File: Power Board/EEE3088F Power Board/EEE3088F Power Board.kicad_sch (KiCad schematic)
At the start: 91 parts, among them J1 Conn_02x16_Odd_Even, J2 USB_C_Receptacle, J3 Conn_01x02_Socket, Q1 2N7002, SW1 SW_SPDT_312, U1 INA219AIDCNR, U10 AP22966DC8-7, U2 LM2596SX-5.0/NOPB, U3 TP4056-42-ESOP8, U4 DRV8837, U5 DRV8837, U6 DRV8837, U8 DRV8837, U9 CH224K

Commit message: more labels and footprints
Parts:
- added JP_M_3V3: 3V3_VM, Jumper:SolderJumper-2_P1.3mm_Open_RoundedPad1.0x1.5mm, symbol Jumper:SolderJumper_2_Open
- D2: value LED -> Red LED; footprint (none) -> LED_SMD:LED_0603_1608Metric_Pad1.05x0.95mm_HandSolder; JLCPCB Part # (none) -> C2286
- D3: value LED -> Green LED; footprint (none) -> LED_SMD:LED_0805_2012Metric_Pad1.15x1.40mm_HandSolder; JLCPCB Part # (none) -> C2297
- L_Bin: renamed from L1; JLCPCB Part # (none) -> C2924827
- renumbered C4 to C_B1, C5 to C_B2, C2 to C_Bin, C3 to C_Bout, C13 to C_C_dd, D1 to D_Bskt, R13 to R_B_LED1, R12 to R_B_LED2, R16 to R_B_b, R14 to R_B_fast, R17 to R_B_pd, R15 to R_B_slow, R23 to R_C_bus, R24 to R_C_cfg, R22 to R_C_dd
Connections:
- net +3V3: now also JP_M_3V3.2 (B); no longer U4.7 (~{SLEEP}), U4.8 (VCC), U5.7 (~{SLEEP}), U5.8 (VCC), U6.7 (~{SLEEP}), U6.8 (VCC), U8.7 (~{SLEEP}), U8.8 (VCC)
- new net 3V3_M: JP_M_3V3.1 (A), U4.7 (~{SLEEP}), U4.8 (VCC), U5.7 (~{SLEEP}), U5.8 (VCC), U6.7 (~{SLEEP}), U6.8 (VCC), U8.7 (~{SLEEP}), U8.8 (VCC)
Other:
- note added: "Do capacitor and inductor values need to be exact? Save budget If so, is it worth changing my whole design to find a different buck convertor that doesn't use extended caps"
- note added: "Done: - Resistors and Capacitors footprints (except LM256) - IC footprints - Schottky diode and 2N7002 footprints - LED footprints To Do: - LM256 caps and inductor? - ask about 0.4R resistor - Neaten net labels - relabel passive components"
- note added: "found a 22uH extended preferred but stock count 307??"
- note removed: "Do capacitor and inductor values need to be exact? Save budget"
- note removed: "Done: - Resistors and Capacitors footprints (except LM256) - IC footprints - Schottky diode and 2N7002 footprints To Do: - LED footprints - LM256 caps and inductor? - ask about 0.4R resistor - Neaten net labels - relabel passive components"
- moved on the sheet: D2, R_B_LED1, U4, U5, U6, U8

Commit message: notes and checked. SW FP to o
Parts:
- removed SW1: SW_SPDT_312, symbol Switch:SW_SPDT_312
- removed TP20: TestPoint, TestPoint:TestPoint_Pad_D2.0mm, symbol Connector:TestPoint
- added JPI4: VIN1, Jumper:SolderJumper-2_P1.3mm_Open_RoundedPad1.0x1.5mm, symbol Jumper:SolderJumper_2_Open
- added JPI5: VIN2, Jumper:SolderJumper-2_P1.3mm_Open_RoundedPad1.0x1.5mm, symbol Jumper:SolderJumper_2_Open
- added JPI6: VBIAS, Jumper:SolderJumper-2_P1.3mm_Open_RoundedPad1.0x1.5mm, symbol Jumper:SolderJumper_2_Open
- added JP_P3: LDO_PWR, Jumper:SolderJumper-2_P1.3mm_Open_RoundedPad1.0x1.5mm, symbol Jumper:SolderJumper_2_Open
- added SW2: ~, ProLib_pcs_2025-03-25:SW-TH_SS-12D11G5, symbol ProLib_pcs_2025-03-25:SS-12D11G5
- C15: footprint Capacitor_SMD:C_0402_1005Metric_Pad0.74x0.62mm_HandSolder -> Capacitor_SMD:C_0603_1608Metric_Pad1.08x0.95mm_HandSolder
- C16: footprint (none) -> Capacitor_SMD:C_0201_0603Metric_Pad0.64x0.40mm_HandSolder
- C25: footprint Capacitor_SMD:C_0402_1005Metric_Pad0.74x0.62mm_HandSolder -> Capacitor_SMD:C_0201_0603Metric_Pad0.64x0.40mm_HandSolder
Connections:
- net +3V3: now also JPI6.2 (B); no longer TP21.1, U10.4 (VBIAS)
- net +5V: now also JPI4.2 (B), JPI5.2 (B), JP_P3.2 (B); no longer C15.1, C25.1, C_P(in)1.2, U10.1_2 (VIN1), U10.6_7 (VIN2), U_P2.3 (VI)
- net Battery: now also SW2.1; no longer JP_P1.2 (B)
- net GND: now also SW2.3
- net Switch-: now also JP_P1.2 (B), SW2.2
- new net: JPI6.1 (A), TP21.1, U10.4 (VBIAS)
- new net: C25.1, JPI4.1 (A), U10.1_2 (VIN1)
- new net: C15.1, JPI5.1 (A), U10.6_7 (VIN2)
- new net: C_P(in)1.2, JP_P3.1 (A), U_P2.3 (VI)
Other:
- note added: "- Double check the Ciss Cap values - Correct symbol - EXT is for base thermal - Add LED indicator."
- note added: "Acceptance Testing - Check shunt res - Vcc solder - Check not overheating - Solder i2c - connect stm Fix: -solder across shunt / replc"
- note added: "Acceptance Testing - solder Boost_mode - solder Boostpwr - Check output tp - Check FB V - Load output Fix: - Change L - Change R"
- note added: "Acceptance Testing - solder PWR - Check output V - LED on - Load output Fix: - Manual 3v3 line - V div"
- note added: "Acceptance testing: - Check correct orientation - Plug in and check V w/ TP Fixing: - Reverse the wires on the batt conn"
- note added: "Acceptance testing: - Solder Vbias - Scheck - Solder VIN1 - CHECK - TOGGLE INPUT - CHECK - repeat EN2 Fixing: - Take the L"
- note added: "Acceptance testing: - With out battery - Check for SC test with multimeter Fixing: - Pull of and solder man"
- note removed: "- Double check the Cap values - What is EXP? Base plate contact maybe - Check this is 100% the right symbol. The other pins are correct, just concerend abt 15 - I think this is the packafe with exposed PAD for thermal - base - Add LED indicator?"
- note removed: "Acceptance Testing - LED will show good power - Test point to measure voltage - Add connection for external load to drive (think Res bank)"

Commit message: added footprints and fixed buck
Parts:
- removed C_Bin: 680uF, symbol Device:C
- removed C_Bout: 220uF, symbol Device:C
- removed D_Bskt: SS54, Diode_SMD:D_SMA, symbol Diode:SS34
- removed JP1: SolderJumper_2_Open, symbol Jumper:SolderJumper_2_Open
- removed L_Bin: 22uH, symbol Device:L
- removed R11: 1, Resistor_SMD:R_0402_1005Metric_Pad0.72x0.64mm_HandSolder, symbol Device:R_US
- removed R18, R21: 0.1R, Resistor_SMD:R_1206_3216Metric_Pad1.30x1.75mm_HandSolder, symbol Device:R_US
- removed TP16, TP5: TestPoint, TestPoint:TestPoint_Pad_D2.0mm, symbol Connector:TestPoint
- removed U2: LM2596SX-5.0/NOPB, LM2596SX-5.0_NOPB:VREG_LM2596SX-5.0_NOPB, symbol Regulator_Switching:LM2596S-5
- added C1: 10uF, Capacitor_SMD:C_1206_3216Metric_Pad1.33x1.80mm_HandSolder, symbol Device:C_Small
- added C2: 10nF, Capacitor_SMD:C_0603_1608Metric_Pad1.08x0.95mm_HandSolder, symbol Device:C_Small
- added C3: 220uF, Capacitor_SMD:CP_Elec_6.3x7.7, symbol Device:C_Small
- added D1: B340, B340A:SMA-DIODE, symbol Diode:B340
- added L1: 18uH, Inductor_SMD:L_Abracon_ASPI-4030S, symbol Device:L_Small
- added R1: 10k, Resistor_SMD:R_0603_1608Metric_Pad0.98x0.95mm_HandSolder, symbol Device:R_Small_US
- added R2: 3k3, Resistor_SMD:R_0603_1608Metric_Pad0.98x0.95mm_HandSolder, symbol Device:R_Small_US
- added U2: TPS5430DDA, Package_SO:SOIC-8-1EP_3.9x4.9mm_P1.27mm_EP2.29x3mm, symbol Regulator_Switching:TPS5430DDA
- D5: footprint (none) -> LED_SMD:LED_0805_2012Metric_Pad1.15x1.40mm_HandSolder
- J1: footprint (none) -> Connector_PinHeader_2.54mm:PinHeader_2x16_P2.54mm_Vertical
- J2: footprint (none) -> Connector_USB:USB_C_Receptacle_G-Switch_GT-USB-7010ASV
- L3: footprint (none) -> Inductor_SMD:L_Changjiang_FXL0630
- R19, R20: value 0.1R -> 1R; footprint Resistor_SMD:R_1206_3216Metric_Pad1.30x1.75mm_HandSolder -> Resistor_SMD:R_0603_1608Metric_Pad0.98x0.95mm_HandSolder
- R_Pfb1: value 732k -> 510k
- R_Pfb2: value 100k -> 68k
- renumbered Batt+ to Batt+1, Batt- to Batt-1, C_C_dd to C_C_dd1, C_I(in) to C_I(in)1, C_P(in) to C_P(in)3, R_B_b to R_B_b1, R_B_fast to R_B_fast1, R_B_pd to R_B_pd1, R_B_slow to R_B_slow1, R_C_bus to R_C_bus1, R_C_cfg to R_C_cfg1, R_C_dd to R_C_dd1, R_Ishunt to R_Ishunt1
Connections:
- net 5V Out is gone; now on net +5V: J1.20 (Pin_20)
- net 5V_Buck_Out: now also R19.1, R20.1, C3.1, L1.2, R1.1; no longer TP17.1
- net GND: now also C1.2, C3.2, D1.2 (A), R2.2, U2.6 (GND), U2.9 (GNDPAD)
- net HV: now also C1.1, U2.7 (VIN)
- net at C_B1.1, D2.2 (A), D3.2 (A)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: now also R19.2, R20.2
- net RESV: no longer names the net of J1.15 (Pin_15)
- net USART2_RX: no longer names the net of J1.9 (Pin_9)
- net USART2_TX: no longer names the net of J1.12 (Pin_12)
- new net: R1.2, R2.1, TP17.1, U2.4 (VSENSE)
- new net: C2.1, U2.1 (BOOT)
- new net: C2.2, D1.1 (K), L1.1, U2.8 (PH)
- no-connect marks 14 -> 18
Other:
- note added: "**fix footprint"
- note added: "Can't find basic 0.4R resistor, can only find basic 1R make 0.5R using parallel"
- note added: "REMEBER TO ASSIGN CORRECT FOOTPRINT"
- note added: "RESV"
- note added: "USART2_RX"
- note added: "USART2_TX"
- note removed: "Can't find basic 0.4R resistor, can only find basic 0.1R"
- note removed: "To copy (Justin values) Foot prints set"
- moved on the sheet: C_B1, C_B2, D2, D3, Q1, R19, R_B_LED1, R_B_LED2, R_B_b1, R_B_fast1, R_B_pd1, R_B_slow1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

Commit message: rip
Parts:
- C16, C25: footprint Capacitor_SMD:C_0201_0603Metric_Pad0.64x0.40mm_HandSolder -> Capacitor_SMD:C_0603_1608Metric_Pad1.08x0.95mm_HandSolder
- SW2: footprint ProLib_pcs_2025-03-25:SW-TH_SS-12D11G5 -> Button_Switch_SMD:SW_SPDT_CK_JS102011SAQN
- U10: footprint AP22966DC8-7:IC_AP22966DC8-7 -> Imported_Files:IC_AP22966DC8-7
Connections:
- net Motor1_A_OUT is gone; now on net MOTOR1_A_OUT: U8.2 (OUT1)
- net Motor1_B_OUT is gone; now on net MOTOR1_B_OUT: U8.3 (OUT2)
- net Motor3_A_OUT is gone; now on net MOTOR3_A_OUT: U6.2 (OUT1)
- net Motor3_B_OUT is gone; now on net MOTOR3_B_OUT: U6.3 (OUT2)
- net MOTOR3_B OUT renamed MOTOR3_A_OUT
- net Motor2_A_OUT renamed MOTOR2_A_OUT
- net Motor2_B_OUT renamed MOTOR2_B_OUT
- net Motor4_A_OUT renamed MOTOR4_A_OUT
- net Motor4_B_OUT renamed MOTOR4_B_OUT
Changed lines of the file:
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@@
 	(text "Do capacitor and inductor values \nneed to be exact? Save budget\nIf so, is it worth changing my whole design \nto find a different buck convertor that \ndoesn't use extended caps"
 		(exclude_from_sim no)
-		(at 214.884 189.992 0)
+		(at 252.476 180.848 0)
 		(effects
 			(font
@@
 	)
 	(junction
-		(at 231.14 187.96)
-		(diameter 0)
-		(color 0 0 0 0)
-	)
-	(junction
 		(at 229.87 57.15)
 		(diameter 0)
@@
 	)
 	(junction
-		(at 269.24 57.15)
-		(diameter 0)
-		(color 0 0 0 0)
-	)
-	(junction
 		(at 386.08 189.23)
 		(diameter 0)
@@
 	(wire
 		(pts
-			(xy 231.14 187.96) (xy 231.14 181.61)
-		)
-		(stroke
-			(width 0)
-			(type default)
-		)
-	)
-	(wire
-		(pts
 			(xy 297.18 149.86) (xy 297.18 151.13)
 		)
@@
 	(wire
 		(pts
-			(xy 269.24 52.07) (xy 269.24 57.15)
-		)
-		(stroke
-			(width 0)
-			(type default)
-		)
-	)
-	(wire
-		(pts
 			(xy 386.08 189.23) (xy 386.08 199.39)
 		)
@@
 	(wire
 		(pts
-			(xy 259.08 57.15) (xy 269.24 57.15)
-		)
-		(stroke
-			(width 0)
-			(type default)
-		)
-	)
-	(wire
-		(pts
 			(xy 464.82 40.64) (xy 464.82 35.56)
 		)
@@
 	(wire
 		(pts
-			(xy 231.14 173.99) (xy 231.14 172.72)
-		)
-		(stroke
-			(width 0)
-			(type default)
-		)
-	)
-	(wire
-		(pts
 			(xy 154.94 179.07) (xy 171.45 179.07)
 		)
@@
 	(wire
 		(pts
-			(xy 231.14 189.23) (xy 231.14 187.96)
-		)
-		(stroke
-			(width 0)
-			(type default)
-		)
-	)
-	(wire
-		(pts
 			(xy 194.31 246.38) (xy 200.66 246.38)
 		)
@@
 	(wire
 		(pts
-			(xy 269.24 57.15) (xy 279.4 57.15)
+			(xy 259.08 57.15) (xy 279.4 57.15)
 		)
 		(stroke
@@
 	(wire
 		(pts
-			(xy 231.14 187.96) (xy 241.3 187.96)
-		)
-		(stroke
-			(width 0)
-			(type default)
-		)
-	)
-	(wire
-		(pts
 			(xy 273.05 143.51) (xy 279.4 143.51)
 		)
@@
 		)
 	)
-	(label "Motor2_B_OUT"
+	(label "MOTOR2_B_OUT"
 		(at 154.94 148.59 0)
 		(effects
@@
 		)
 	)
-	(label "3V3 Out"
-		(at 269.24 52.07 0)
-		(effects
-			(font
-				(size 1.27 1.27)
-			)
-			(justify left bottom)
-		)
-	)
-	(label "Motor1_A_OUT"
+	(label "MOTOR1_A_OUT"
 		(at 482.6 92.71 0)
 		(effects
@@
 		)
 	)
-	(label "MOTOR3_B OUT"
+	(label "MOTOR3_A_OUT"
 		(at 156.21 181.61 0)
 		(effects
@@
 		)
 	)
-	(label "Motor4_B_OUT"
+	(label "MOTOR4_B_OUT"
 		(at 553.72 59.69 0)
 		(effects
@@
 		)
 	)
-	(label "Motor2_B_OUT"
+	(label "MOTOR2_B_OUT"
 		(at 481.33 60.96 0)
 		(effects
@@
 		)
 	)
-	(label "Motor3_B_OUT"
+	(label "MOTOR3_B_OUT"
 		(at 554.99 105.41 0)
 		(effects
@@
 		)
 	)
-	(label "Motor1_B_OUT"
+	(label "MOTOR1_B_OUT"
 		(at 482.6 107.95 0)
 		(effects
@@
 		)
 	)
-	(label "Motor2_A_OUT"
+	(label "MOTOR2_A_OUT"
 		(at 490.22 45.72 0)
 		(effects
@@
 		)
 	)
-	(label "Motor2_A_OUT"
+	(label "MOTOR2_A_OUT"
 		(at 186.69 148.59 0)
 		(effects
@@
 		)
 	)
-	(label "Motor3_A_OUT"
+	(label "MOTOR3_A_OUT"
 		(at 554.99 90.17 0)
 		(effects
@@
 		)
 	)
-	(label "Motor4_A_OUT"
+	(label "MOTOR4_A_OUT"
 		(at 562.61 44.45 0)
 		(effects
@@
 		)
 	)
-	(label "Motor4_A_OUT"
+	(label "MOTOR4_A_OUT"
 		(at 154.94 151.13 0)
 		(effects
@@
 			)
 		)
-		(property "Footprint" "ProLib_pcs_2025-03-25:SW-TH_SS-12D11G5"
+		(property "Footprint" "Button_Switch_SMD:SW_SPDT_CK_JS102011SAQN"
 			(at 69.85 327.66 0)
 			(effects
@@
 			)
 		)
-		(property "Footprint" "AP22966DC8-7:IC_AP22966DC8-7"
+		(property "Footprint" "Imported_Files:IC_AP22966DC8-7"
 			(at 71.12 238.76 0)
 			(effects
@@
 	)
 	(symbol
-		(lib_id "power:GND")
-		(at 231.14 189.23 0)
-		(unit 1)
-		(exclude_from_sim no)
-		(in_bom yes)
-		(on_board yes)
-		(dnp no)
-		(fields_autoplaced yes)
-		(property "Reference" "#PWR04"
-			(at 231.14 195.58 0)
-			(effects
-				(font
-					(size 1.27 1.27)
-				)
-				(hide yes)
-			)
-		)
-		(property "Value" "GND"
-			(at 231.14 194.31 0)
-			(effects
-				(font
-					(size 1.27 1.27)
-				)
-			)
-		)
-		(property "Footprint" ""
-			(at 231.14 189.23 0)
-			(effects
-				(font
-					(size 1.27 1.27)
-				)
-				(hide yes)
-			)
-		)
-		(property "Datasheet" ""
-			(at 231.14 189.23 0)
-			(effects
-				(font
-					(size 1.27 1.27)
-				)
-				(hide yes)
-			)
-		)
-		(property "Description" "Power symbol creates a global label with name \"GND\" , ground"
-			(at 231.14 189.23 0)
-			(effects
-				(font
-					(size 1.27 1.27)
-				)
-				(hide yes)
-			)
-		)
-		(pin "1"
-		)
-		(instances
-			(project ""
-				(path "/713ead88-0bd2-43ee-981f-e11872ed406d"
-					(reference "#PWR04")
-					(unit 1)
-				)
-			)
-		)
-	)
-	(symbol
 		(lib_id "Device:L")
 		(at 95.25 50.8 90)
@@
 			)
 		)
-		(property "Footprint" "Capacitor_SMD:C_0201_0603Metric_Pad0.64x0.40mm_HandSolder"
+		(property "Footprint" "Capacitor_SMD:C_0603_1608Metric_Pad1.08x0.95mm_HandSolder"
 			(at 96.52 233.68 0)
 			(effects
@@
 			)
 		)
-		(property "Footprint" "Capacitor_SMD:C_0201_0603Metric_Pad0.64x0.40mm_HandSolder"
+		(property "Footprint" "Capacitor_SMD:C_0603_1608Metric_Pad1.08x0.95mm_HandSolder"
 			(at 21.59 233.68 0)
 			(effects

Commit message: Fixed communal fp and symbols
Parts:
- removed SW2: ~, Button_Switch_SMD:SW_SPDT_CK_JS102011SAQN, symbol ProLib_pcs_2025-03-25:SS-12D11G5
- removed U10: AP22966DC8-7, Imported_Files:IC_AP22966DC8-7, symbol AP22966DC8-7:AP22966DC8-7
- added SW1: ~, custom_footprints:SW-TH_SS-12D11G5, symbol Custom_symbols:SS-12D11G5
- added U7: AP22966DC8-7, custom_footprints:IC_AP22966DC8-7, symbol Custom_symbols:AP22966DC8-7
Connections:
- net Battery: now also SW1.1
- net CTRL_EXT_LOAD1: now also U7.3 (EN1)
- net CTRL_EXT_LOAD2: now also U7.5 (EN2)
- net EXT_LOAD1_OUT: now also U7.13_14 (VOUT1)
- net EXT_LOAD2_OUT: now also U7.8_9 (VOUT2)
- net GND: now also SW1.3, U7.11 (GND), U7.15 (EXP)
- net Switch-: now also SW1.2
- net at JPI6.1 (A), TP21.1: now also U7.4 (VBIAS)
- net at C17.2: now also U7.10 (SS2)
- net at C16.2: now also U7.12 (SS1)
- net at C25.1, JPI4.1 (A): now also U7.1_2 (VIN1)
- net at C15.1, JPI5.1 (A): now also U7.6_7 (VIN2)

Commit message: ELC checks
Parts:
- D1: footprint B340A:SMA-DIODE -> custom_footprints:SMA-DIODE
- U3: footprint TP4056-42-ESOP8:SOIC127P600X175-9N -> custom_footprints:SOIC127P600X175-9N
- U4, U5, U6, U8: footprint DRV8837DSGR:SON50P200X200X80-9N -> custom_footprints:SON50P200X200X80-9N
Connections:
- net +3V3 is gone; now on net +3.3V: C_P(in)2.2, J1.18 (Pin_18), JPI6.2 (B), JP_M_3V3.2 (B), R_P2.1, TP_P6.1, U_P2.2 (VO)
- net MOTOR4_B_OUT_ is gone; now on net MOTOR4_B_OUT: J1.5 (Pin_5)
- net HV: no longer J1.22 (Pin_22), J2.A4 (VBUS), J2.A9 (VBUS), J2.B4 (VBUS), J2.B9 (VBUS), R_C_bus1.1, R_C_dd1.1, TP6.1
- new net +9V: J1.22 (Pin_22), J2.A4 (VBUS), J2.A9 (VBUS), J2.B4 (VBUS), J2.B9 (VBUS), R_C_bus1.1, R_C_dd1.1, TP6.1

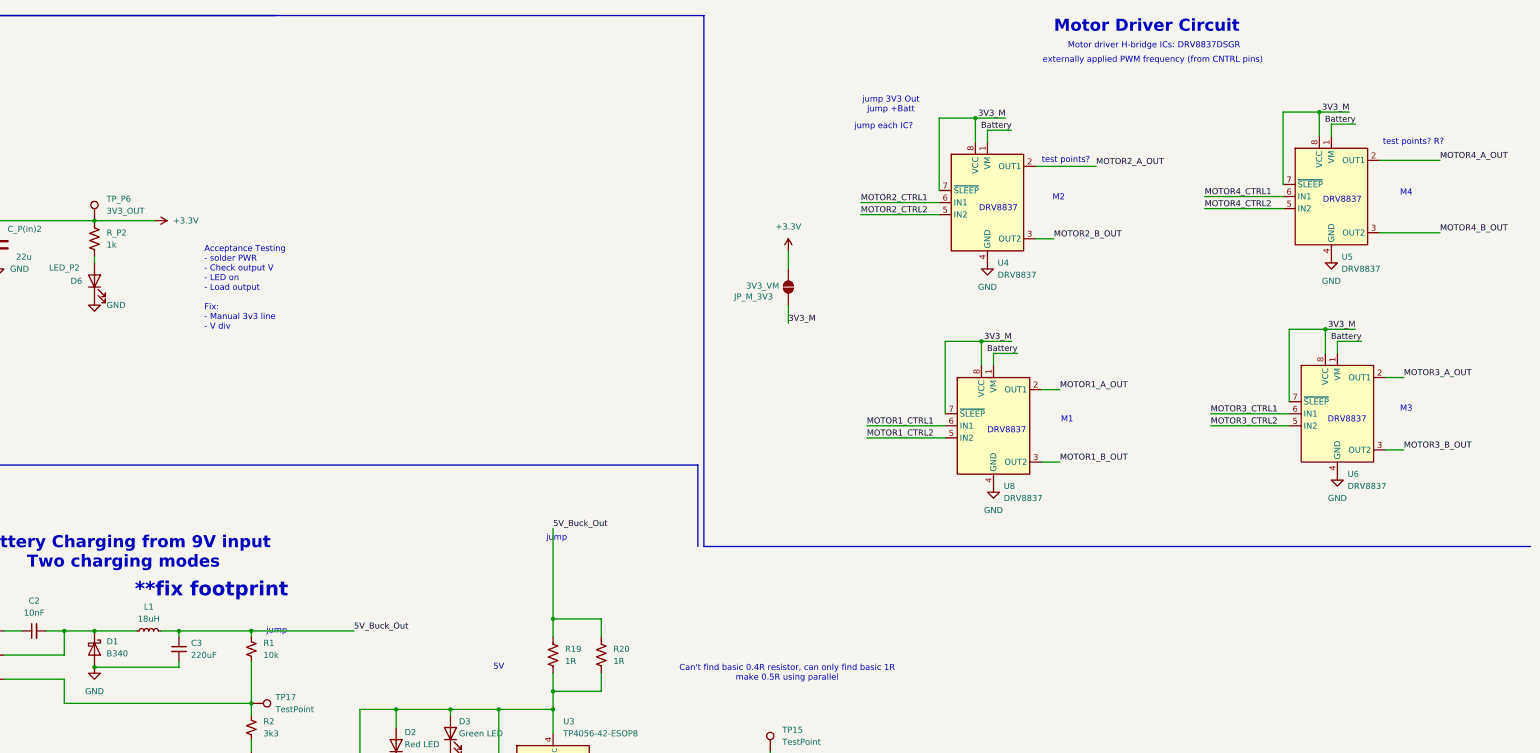
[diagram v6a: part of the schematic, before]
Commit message: fixed footprints and symbols
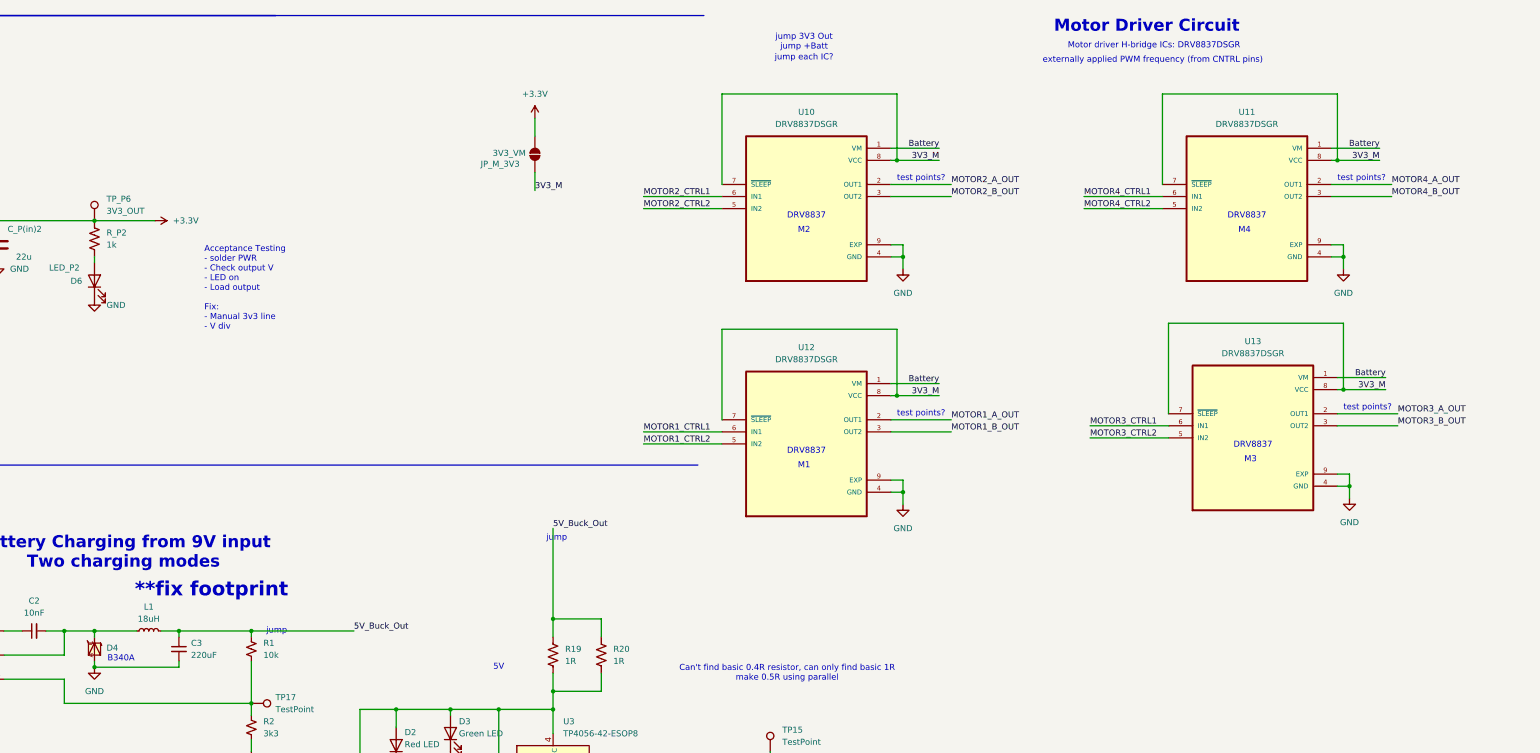
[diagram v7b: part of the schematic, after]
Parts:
- removed D1: B340, custom_footprints:SMA-DIODE, symbol Diode:B340
- removed U4, U5, U6, U8: DRV8837, custom_footprints:SON50P200X200X80-9N, symbol Driver_Motor:DRV8837
- added D4: BA340A, custom_footprints:SMA-DIODE, symbol Custom_symbols:B340A
- added U10, U11, U12, U13: DRV8837DSGR, custom_footprints:SON50P200X200X80-9N, symbol Custom_symbols:DRV8837DSGR
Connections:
- net 3V3_M: now also U10.7 (~{SLEEP}), U10.8 (VCC), U11.7 (~{SLEEP}), U11.8 (VCC), U12.7 (~{SLEEP}), U12.8 (VCC), U13.7 (~{SLEEP}), U13.8 (VCC)
- net Battery: now also U10.1 (VM), U11.1 (VM), U12.1 (VM), U13.1 (VM)
- net GND: now also D4.A, U10.4 (GND), U10.9 (EXP), U11.4 (GND), U11.9 (EXP), U12.4 (GND), U12.9 (EXP), U13.4 (GND), U13.9 (EXP)
- net MOTOR1_A_OUT: now also U12.2 (OUT1)
- net MOTOR1_B_OUT: now also U12.3 (OUT2)
- net MOTOR1_CTRL1: now also U12.6 (IN1)
- net MOTOR1_CTRL2: now also U12.5 (IN2)
- net MOTOR2_A_OUT: now also U10.2 (OUT1)
- net MOTOR2_B_OUT: now also U10.3 (OUT2)
- net MOTOR2_CTRL1: now also U10.6 (IN1)
- net MOTOR2_CTRL2: now also U10.5 (IN2)
- net MOTOR3_A_OUT: now also U13.2 (OUT1)
- net MOTOR3_B_OUT: now also U13.3 (OUT2)
- net MOTOR3_CTRL1: now also U13.6 (IN1)
- net MOTOR3_CTRL2: now also U13.5 (IN2)
- net MOTOR4_A_OUT: now also U11.2 (OUT1)
- net MOTOR4_B_OUT: now also U11.3 (OUT2)
- net MOTOR4_CTRL1: now also U11.6 (IN1)
- net MOTOR4_CTRL2: now also U11.5 (IN2)
- net at C2.2, L1.1, U2.8 (PH): now also D4.C
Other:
- note added: "B340A"
- note removed: "test points? R?"
- moved on the sheet: JP_M_3V3

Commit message: still no footprints on pcb editor (mac error)
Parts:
- renumbered C3 to C_B3, C2 to C_Bboot1, C1 to C_Bin1, R1 to R_Bset1, R2 to R_Bset2
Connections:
- net HV is gone; now on net +9V: C_Bin1.1, U2.7 (VIN)
- net +3.3V: no longer C_P(in)2.2, R_P2.1, TP_P6.1, U_P2.2 (VO)
- net Batt+: no longer Batt+1.1, J3.1 (Pin_1)
- net -BATT: now reaches Batt-1.1, J3.2 (Pin_2)
- new net: C_P(in)2.2, R_P2.1, TP_P6.1, U_P2.2 (VO)
- new net +BATT: Batt+1.1, J3.1 (Pin_1)
- no-connect marks 18 -> 20
